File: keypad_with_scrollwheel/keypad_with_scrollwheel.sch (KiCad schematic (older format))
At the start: 30 parts, among them U1 KEYPAD_OVERLAY

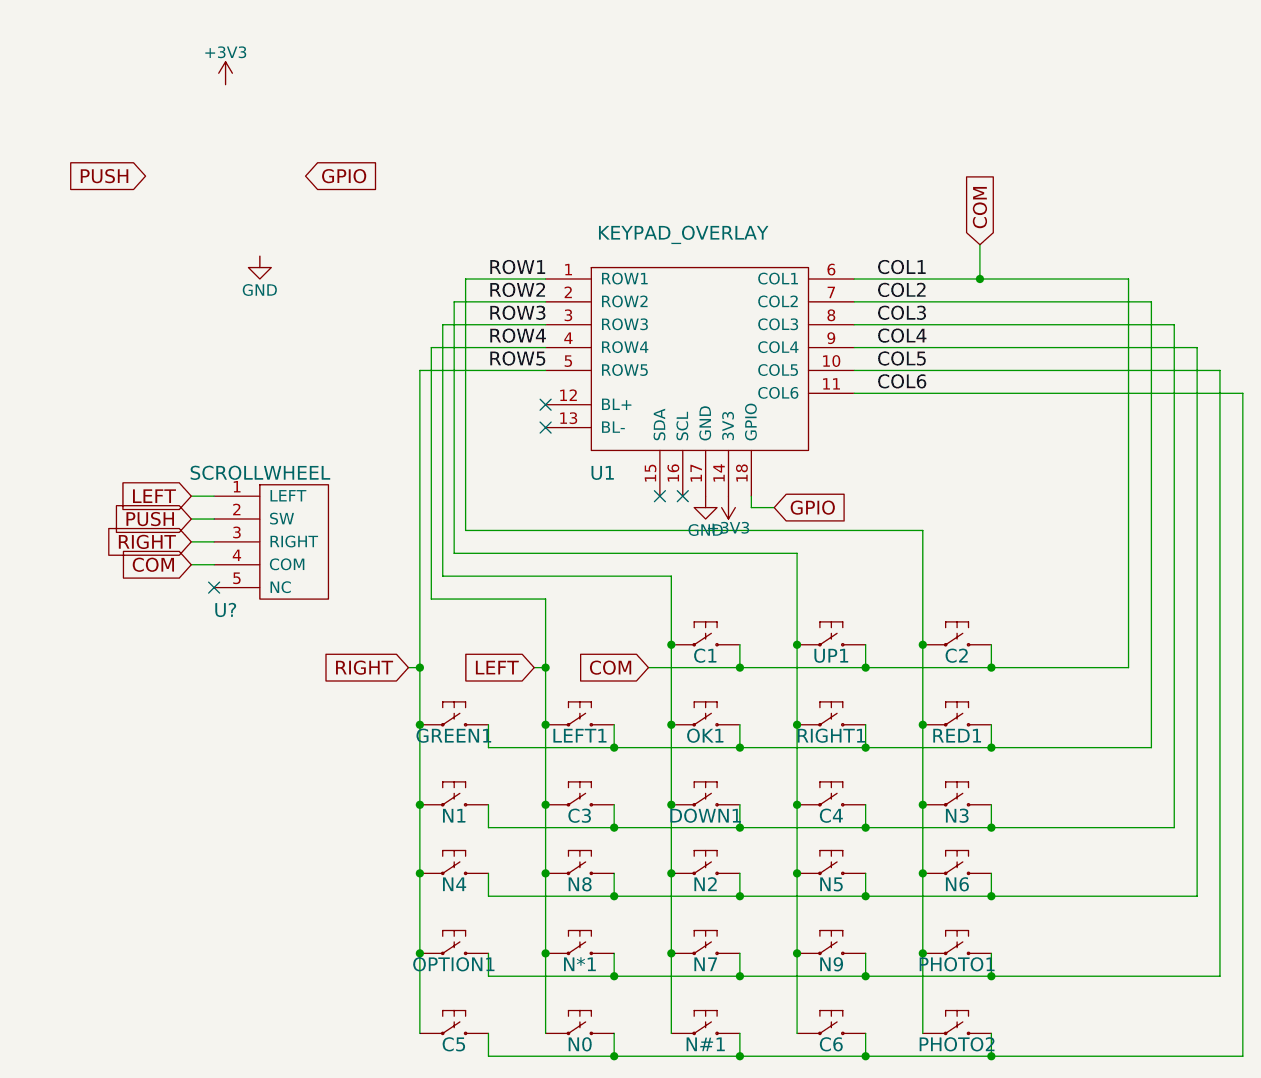
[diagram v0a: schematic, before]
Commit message: Finished the keypad+scrollwheel board - needs to be printed out
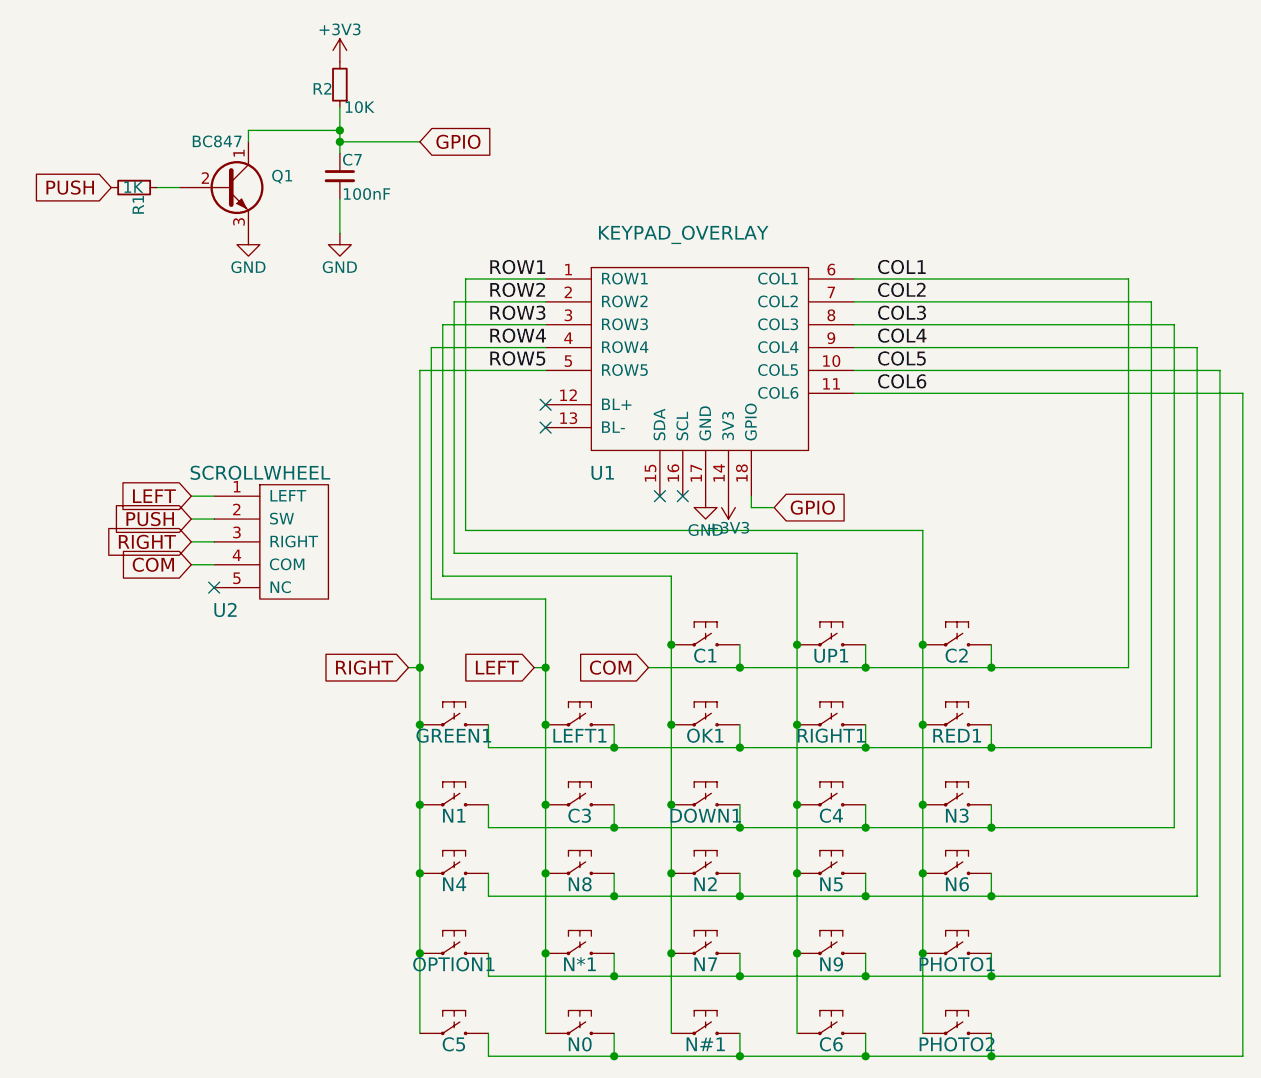
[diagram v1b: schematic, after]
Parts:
- added C7: 100nF, Capacitors_SMD:C_0805, symbol C_Small
- added Q1: BC847, TO_SOT_Packages_SMD:SOT-23_Handsoldering, symbol Q_NPN_CBE
- added R1: 1K, Resistors_SMD:R_0805_HandSoldering, symbol R_Small
- added R2: 10K, Resistors_SMD:R_0805_HandSoldering, symbol R_Small
- U1: footprint (none) -> footprints:keypad_overlay
- U2: renamed from U?; footprint (none) -> footprints:SCROLLWHEEL
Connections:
- net +3V3: now also R2.2
- net GND: now also C7.2, Q1.3 (E)
- net GPIO: now also C7.1, Q1.1 (C), R2.1
- net PUSH: now also R1.2
- new net: Q1.2 (B), R1.1
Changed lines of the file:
@@
 LIBS:valves
 LIBS:scrollwheel
+LIBS:keypad_overlay
 LIBS:keypad_with_scrollwheel-cache
 EELAYER 25 0
@@
 F 0 "U1" H 3300 1450 60  0000 C CNN
 F 1 "KEYPAD_OVERLAY" H 3650 2500 60  0000 C CNN
-F 2 "" H 3850 2100 60  0001 C CNN
+F 2 "footprints:keypad_overlay" H 3850 2100 60  0001 C CNN
 F 3 "" H 3850 2100 60  0001 C CNN
 	1    3850 2100
@@
 ROW5
 $Comp
-L SCROLLWHEEL U?
+L SCROLLWHEEL U2
 U 1 1 59A4B31B
 P 1900 3050
-F 0 "U?" H 1650 2750 60  0000 C CNN
+F 0 "U2" H 1650 2750 60  0000 C CNN
 F 1 "SCROLLWHEEL" H 1800 3350 60  0000 C CNN
-F 2 "" H 2200 2850 60  0001 C CNN
+F 2 "footprints:SCROLLWHEEL" H 2200 2850 60  0001 C CNN
 F 3 "" H 2200 2850 60  0001 C CNN
 	1    1900 3050
 	1    0    0    -1
 $EndComp
-Text GLabel 4950 1750 1    60   Input ~ 0
-COM
 Text GLabel 1500 3150 0    60   Input ~ 0
 COM
@@
 Wire Wire Line
 	2500 2300 2500 5200
-Connection ~ 4950 1900
-Wire Wire Line
-	4950 1750 4950 1900
 Wire Wire Line
 	1600 3150 1500 3150
@@
 Connection ~ 3050 3600
 $Comp
-L GND #PWR?
+L GND #PWR01
 U 1 1 59A4CBB3
 P 3750 2850
-F 0 "#PWR?" H 3750 2600 50  0001 C CNN
+F 0 "#PWR01" H 3750 2600 50  0001 C CNN
 F 1 "GND" H 3750 2700 50  0000 C CNN
 F 2 "" H 3750 2850 50  0001 C CNN
@@
 $EndComp
 $Comp
-L +3V3 #PWR?
+L +3V3 #PWR02
 U 1 1 59A4CC03
 P 3850 2850
-F 0 "#PWR?" H 3850 2700 50  0001 C CNN
+F 0 "#PWR02" H 3850 2700 50  0001 C CNN
 F 1 "+3V3" H 3850 2990 50  0000 C CNN
 F 2 "" H 3850 2850 50  0001 C CNN
@@
 Wire Wire Line
 	3950 2900 3950 2850
-Text GLabel 1300 1450 0    60   Input ~ 0
+Text GLabel 1150 1500 0    60   Input ~ 0
 PUSH
-Text GLabel 2000 1450 2    60   Input ~ 0
+Text GLabel 2500 1300 2    60   Input ~ 0
 GPIO
 $Comp
-L GND #PWR?
+L GND #PWR03
 U 1 1 59A4D274
-P 1800 1800
-F 0 "#PWR?" H 1800 1550 50  0001 C CNN
-F 1 "GND" H 1800 1650 50  0000 C CNN
-F 2 "" H 1800 1800 50  0001 C CNN
-F 3 "" H 1800 1800 50  0001 C CNN
-	1    1800 1800
-	1    0    0    -1
-$EndComp
-$Comp
-L +3V3 #PWR?
+P 1750 1700
+F 0 "#PWR03" H 1750 1450 50  0001 C CNN
+F 1 "GND" H 1750 1550 50  0000 C CNN
+F 2 "" H 1750 1700 50  0001 C CNN
+F 3 "" H 1750 1700 50  0001 C CNN
+	1    1750 1700
+	1    0    0    -1
+$EndComp
+$Comp
+L +3V3 #PWR04
 U 1 1 59A4D351
-P 1650 1050
-F 0 "#PWR?" H 1650 900 50  0001 C CNN
-F 1 "+3V3" H 1650 1190 50  0000 C CNN
-F 2 "" H 1650 1050 50  0001 C CNN
-F 3 "" H 1650 1050 50  0001 C CNN
-	1    1650 1050
-	1    0    0    -1
-$EndComp
+P 2150 950
+F 0 "#PWR04" H 2150 800 50  0001 C CNN
+F 1 "+3V3" H 2150 1090 50  0000 C CNN
+F 2 "" H 2150 950 50  0001 C CNN
+F 3 "" H 2150 950 50  0001 C CNN
+	1    2150 950
+	1    0    0    -1
+$EndComp
+$Comp
+L Q_NPN_CBE Q1
+U 1 1 5A888DC4
+P 1650 1500
+F 0 "Q1" H 1850 1550 50  0000 L CNN
+F 1 "BC847" H 1500 1700 50  0000 L CNN
+F 2 "TO_SOT_Packages_SMD:SOT-23_Handsoldering" H 1850 1600 50  0001 C CNN
+F 3 "" H 1650 1500 50  0001 C CNN
+	1    1650 1500
+	1    0    0    -1
+$EndComp
+$Comp
+L R_Small R1
+U 1 1 5A889176
+P 1250 1500
+F 0 "R1" H 1280 1520 50  0000 L CNN
+F 1 "1K" V 1250 1450 50  0000 L CNN
+F 2 "Resistors_SMD:R_0805_HandSoldering" H 1250 1500 50  0001 C CNN
+F 3 "" H 1250 1500 50  0001 C CNN
+	1    1250 1500
+	0    1    1    0
+$EndComp
+$Comp
+L C_Small C7
+U 1 1 5A88923F
+P 2150 1450
+F 0 "C7" H 2160 1520 50  0000 L CNN
+F 1 "100nF" H 2160 1370 50  0000 L CNN
+F 2 "Capacitors_SMD:C_0805" H 2150 1450 50  0001 C CNN
+F 3 "" H 2150 1450 50  0001 C CNN
+	1    2150 1450
+	1    0    0    -1
+$EndComp
+$Comp
+L GND #PWR05
+U 1 1 5A8892C9
+P 2150 1700
+F 0 "#PWR05" H 2150 1450 50  0001 C CNN
+F 1 "GND" H 2150 1550 50  0000 C CNN
+F 2 "" H 2150 1700 50  0001 C CNN
+F 3 "" H 2150 1700 50  0001 C CNN
+	1    2150 1700
+	1    0    0    -1
+$EndComp
+$Comp
+L R_Small R2
+U 1 1 5A88939C
+P 2150 1050
+F 0 "R2" H 2180 1070 50  0000 L CNN
+F 1 "10K" H 2000 1150 50  0000 L CNN
+F 2 "Resistors_SMD:R_0805_HandSoldering" H 2150 1050 50  0001 C CNN
+F 3 "" H 2150 1050 50  0001 C CNN
+	1    2150 1050
+	-1   0    0    1
+$EndComp
+Wire Wire Line
+	2150 1150 2150 1350
+Wire Wire Line
+	2150 1300 2500 1300
+Connection ~ 2150 1300
+Wire Wire Line
+	1750 1300 1750 1250
+Wire Wire Line
+	1750 1250 2150 1250
+Connection ~ 2150 1250
+Wire Wire Line
+	2150 1550 2150 1700
+Wire Wire Line
+	1350 1500 1450 1500
 $EndSCHEMATC
